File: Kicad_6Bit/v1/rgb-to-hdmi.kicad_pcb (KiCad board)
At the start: 2 copper layers, 65 x 30 mm, 30 parts, among them P1 CONN_02X20, P2 Conn_02x05_Odd_Even, P3 Conn_01x06, P4 CONN_01X02, SW1 SW_PUSH, SW2 SW_PUSH, SW3 SW_PUSH, SW4 SW_PUSH, U1 XC9572XL-VQFP44

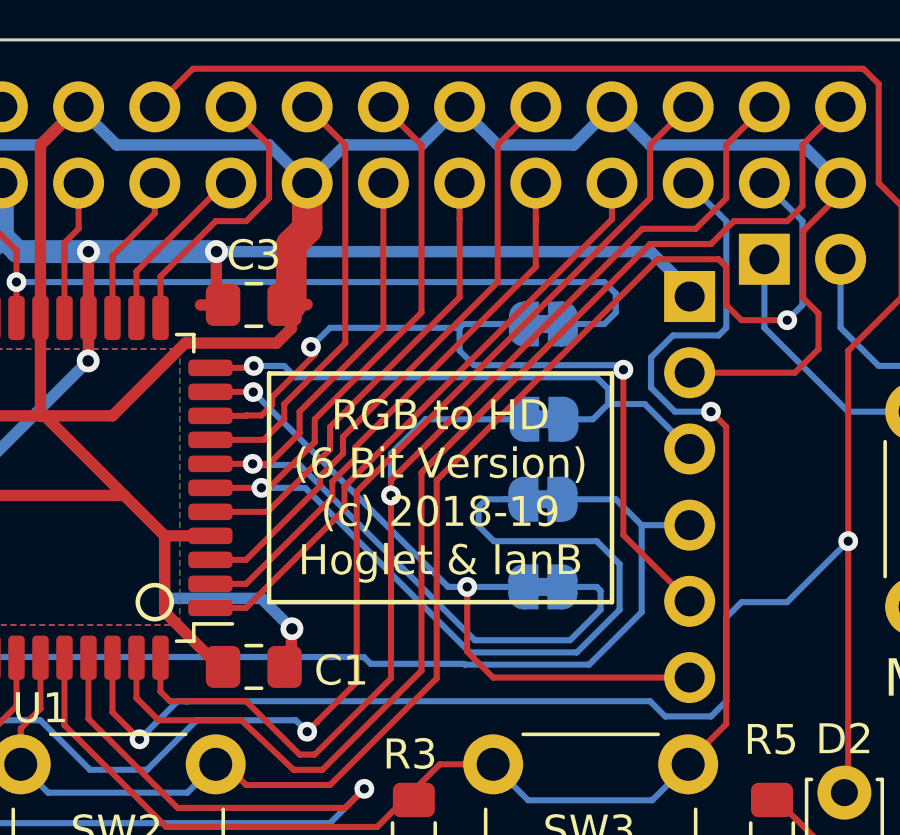
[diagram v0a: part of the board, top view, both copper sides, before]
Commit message: Fix incorrect in system programming GPIO assignments
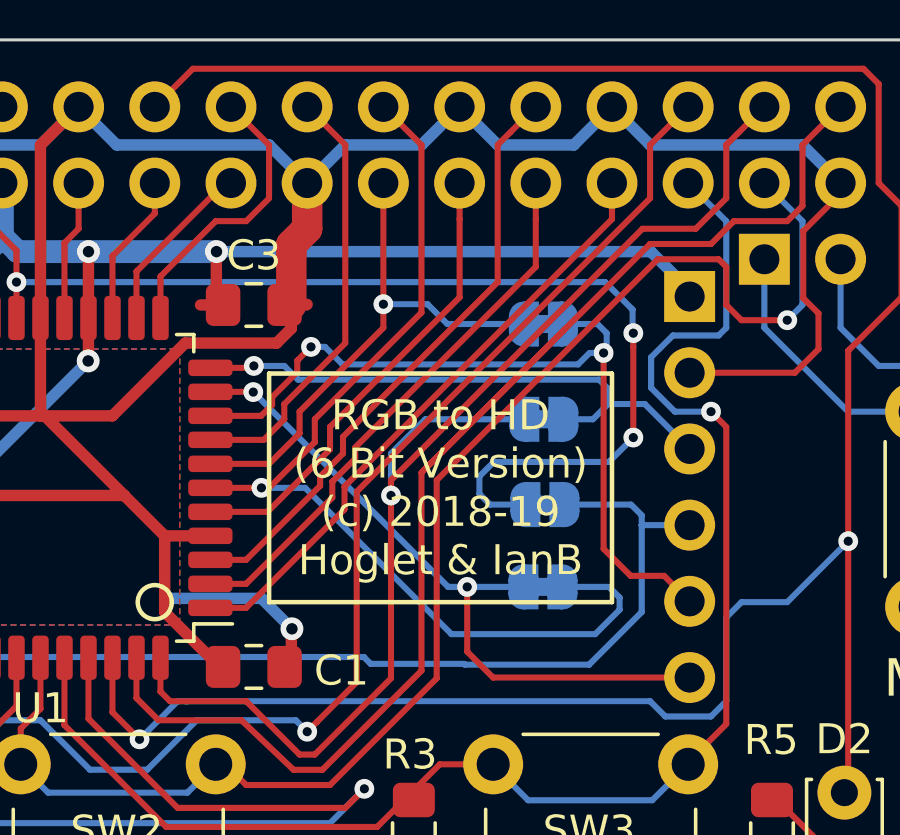
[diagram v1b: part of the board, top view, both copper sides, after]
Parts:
- moved JP3 0.19 mm to (59.3, 40.0)
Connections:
- JP1 pad 1: /TDI -> /GPIO0
- JP1 pad 2: /GPIO24 -> /TDI
- JP3 pad 1: /GPIO1 -> /GPIO24
- JP4 pad 2: /GPIO0 -> /GPIO1
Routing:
- net /GPIO0: track 29.1 -> 17.9 mm
- net /GPIO24: track 30.8 -> 41.2 mm, vias 1 -> 3
- net /GPIO1: track 40.9 -> 33.9 mm

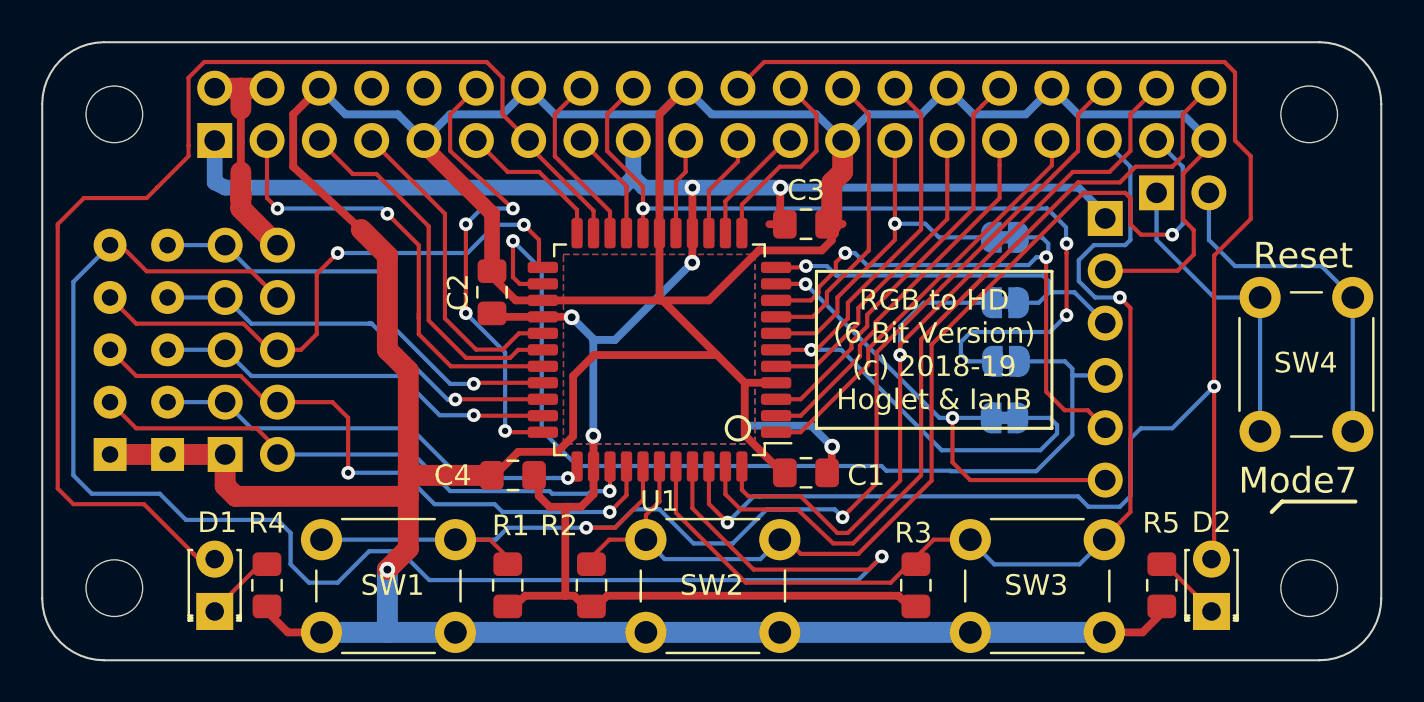
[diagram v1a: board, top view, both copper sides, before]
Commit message: Move some vias to avoid shorting hazard with IDC cable
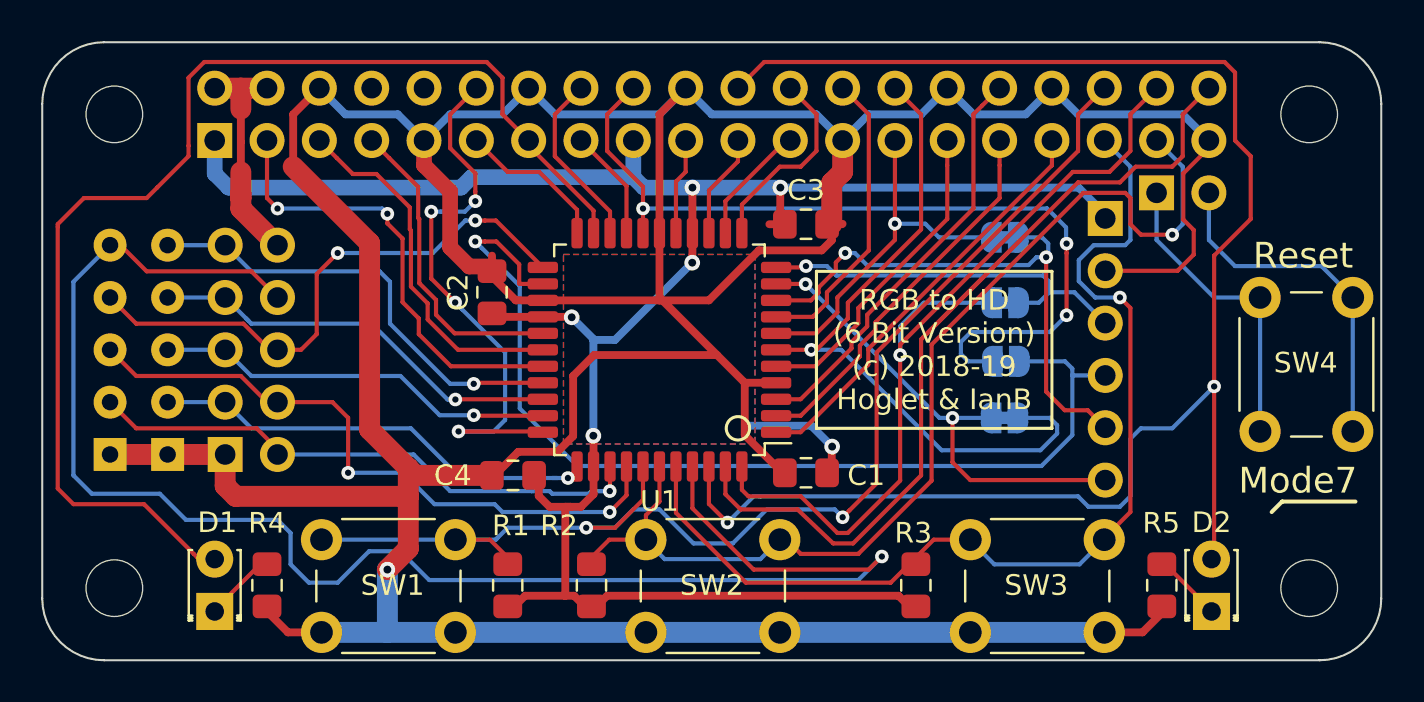
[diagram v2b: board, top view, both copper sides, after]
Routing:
- net /GPIO18: track 22.8 -> 27.1 mm
- net /TDO: track 47.8 -> 49.6 mm
- net /GND: track 226.5 -> 227.3 mm
- net /GPIO4: track 16.1 -> 15.6 mm

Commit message: Fix GND plane plus other minor tweaks
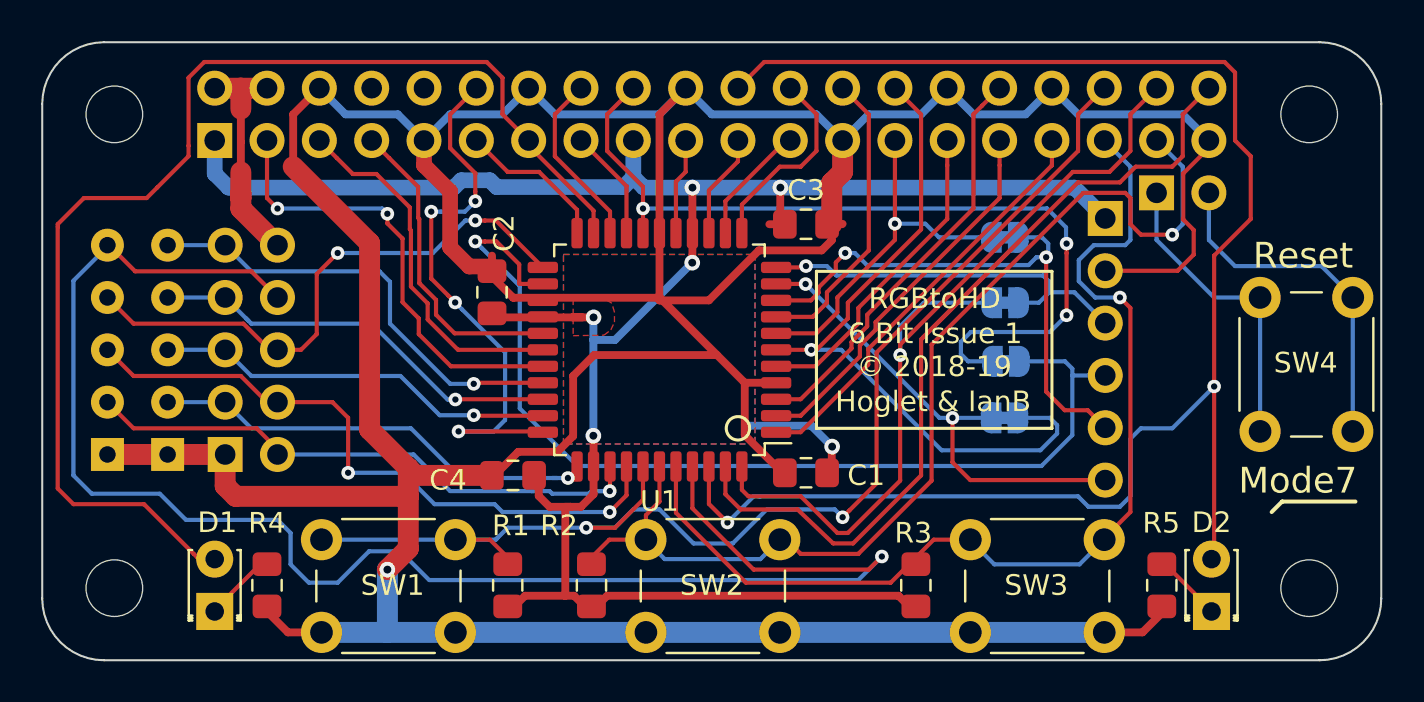
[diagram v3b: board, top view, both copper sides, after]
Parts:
- moved RN2 0.13 mm to (15.7, 44.5)
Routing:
- net /3V3: track 110.5 -> 111.9 mm
- added copper zone on F.Cu, net /GND
- removed copper zone on F.Cu, net GND
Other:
- board text added: "6 Bit Issue 1"
- board text added: "Hoglet & IanB"
- board text added: "RGBtoHD"
- board text added: "© 2018-19"
- board text removed: "RGB to HD (6 Bit Version) (c) 2018-19 Hoglet & IanB"

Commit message: Swap JP4, change P3 side & add more silk screen info
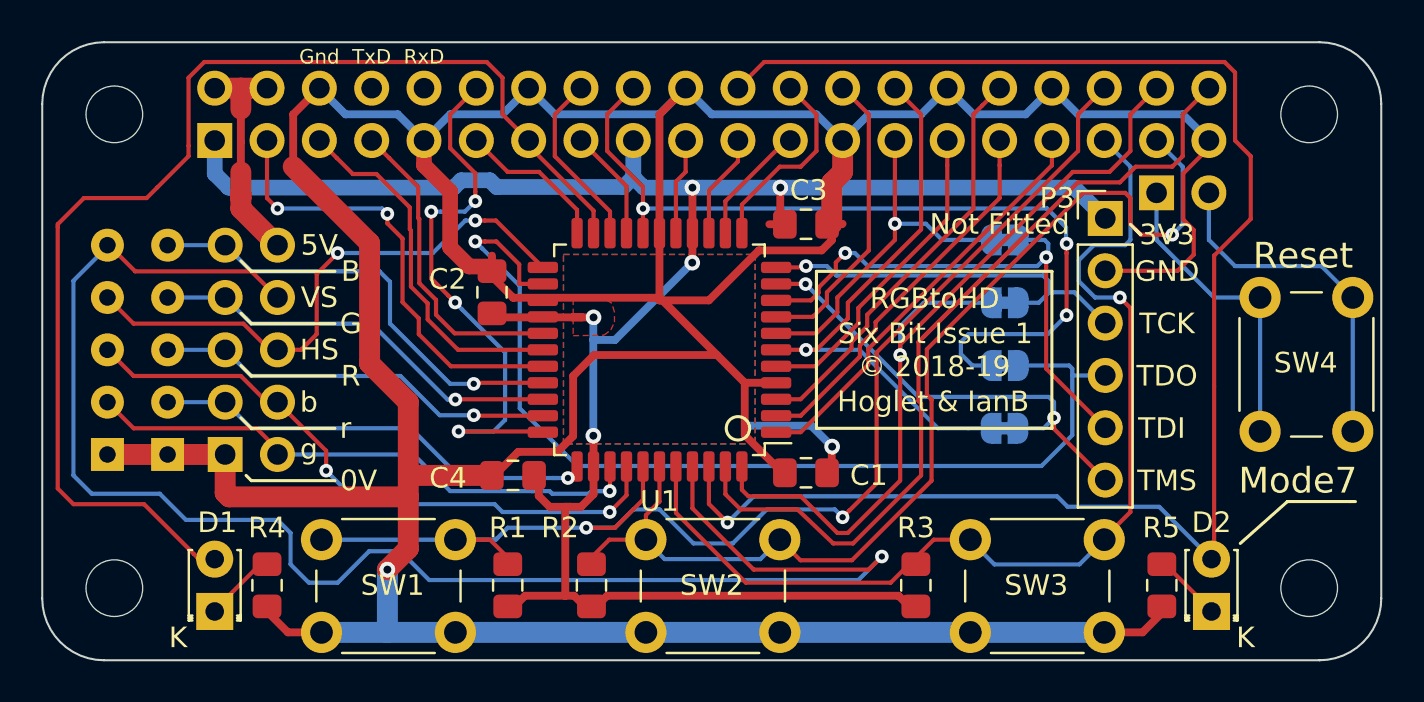
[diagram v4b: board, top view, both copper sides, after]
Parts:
- P3: moved to F.Cu
- moved JP4 0.51 mm to (59.2, 43.2)
- moved JP3 0.21 mm to (59.2, 40.2)
- moved JP1 0.13 mm to (59.2, 34.1)
- turned P3 to 0 degrees
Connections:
- JP4 pad 1: /TMS -> /GPIO1
- JP4 pad 2: /GPIO1 -> /TMS
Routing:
- net /GPIO1: track 33.9 -> 27.7 mm
- net /GPIO25: track 80.9 -> 77.6 mm, vias 2 -> 1
- net /BBLUE: track 31.5 -> 30.0 mm
- net /GND: track 227.3 -> 228.3 mm
- net /TDI: track 27.7 -> 27.0 mm
- net /TMS: track 23.0 -> 22.5 mm
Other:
- board text added: "0V"
- board text added: "3V3"
- board text added: "5V"
- board text added: "B"
- board text added: "G"
- board text added: "GND"
- board text added: "Gnd"
- board text added: "HS"
- board text added: "K"
- board text added: "R"
- board text added: "RxD"
- board text added: "Six Bit Issue 1"
- board text added: "TCK"
- board text added: "TDI"
- board text added: "TDO"
- board text added: "TMS"
- board text added: "TxD"
- board text added: "VS"
- board text added: "b"
- board text added: "g"
- board text added: "r"
- board text removed: "6 Bit Issue 1"

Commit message: Tweaks to vias and silk screen
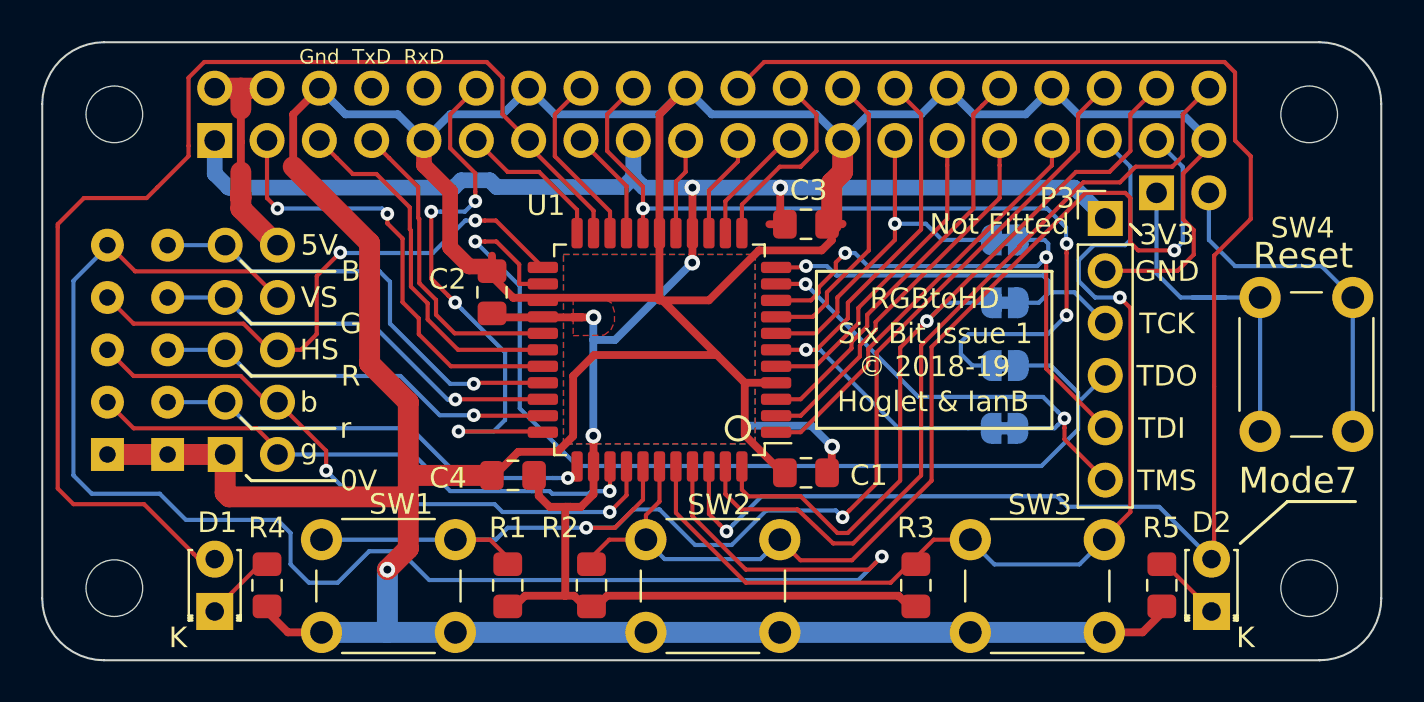
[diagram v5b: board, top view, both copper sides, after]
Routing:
- net /GPIO21: track 46.5 -> 39.7 mm
- net /GPIO20: track 42.4 -> 38.9 mm
- net Net-(P4-Pad1): track 15.4 -> 17.9 mm
- net /GPIO26: track 51.9 -> 53.3 mm
- net /GPIO25: track 77.6 -> 78.3 mm
